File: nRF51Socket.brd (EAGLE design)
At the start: 46 x 41 mm, 11 parts, among them U1 QFN-48(52)BT-0.4-01-00, X1 16MHz

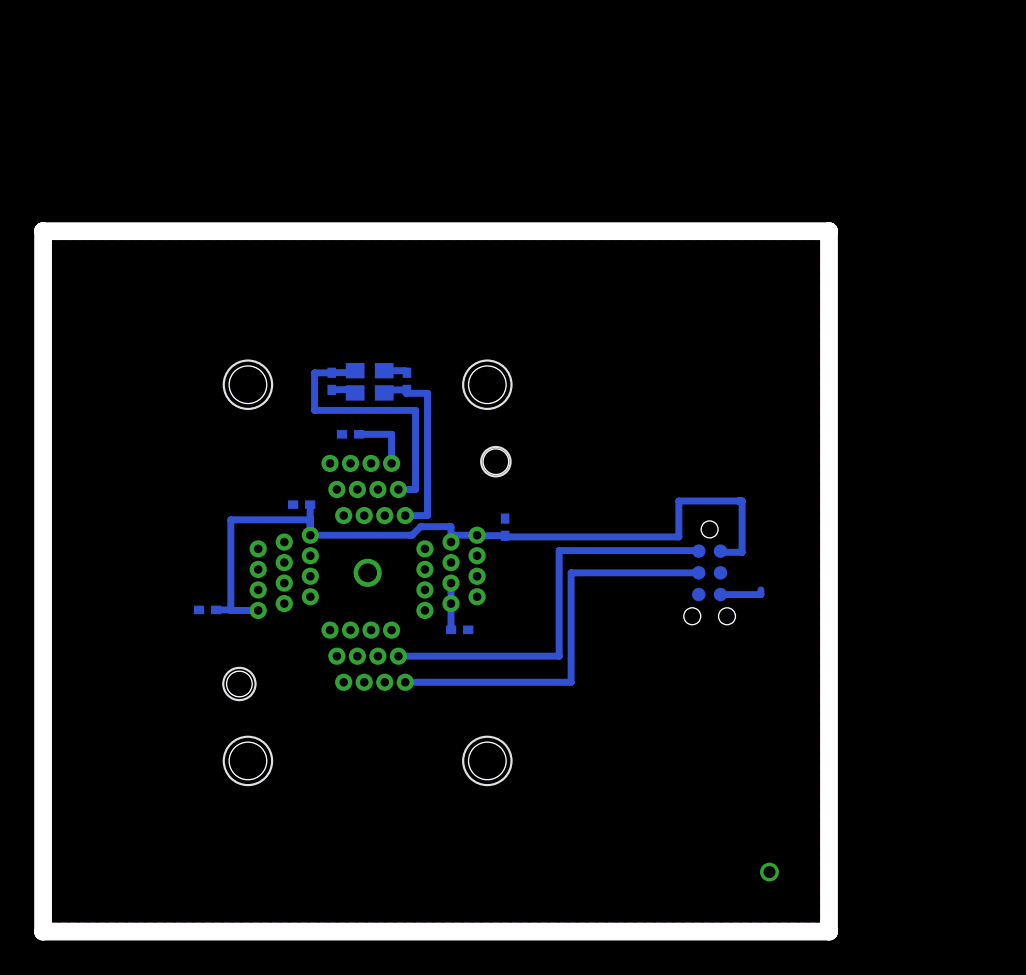
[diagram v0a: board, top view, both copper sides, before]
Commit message: Changed to 20pin jtag socket.
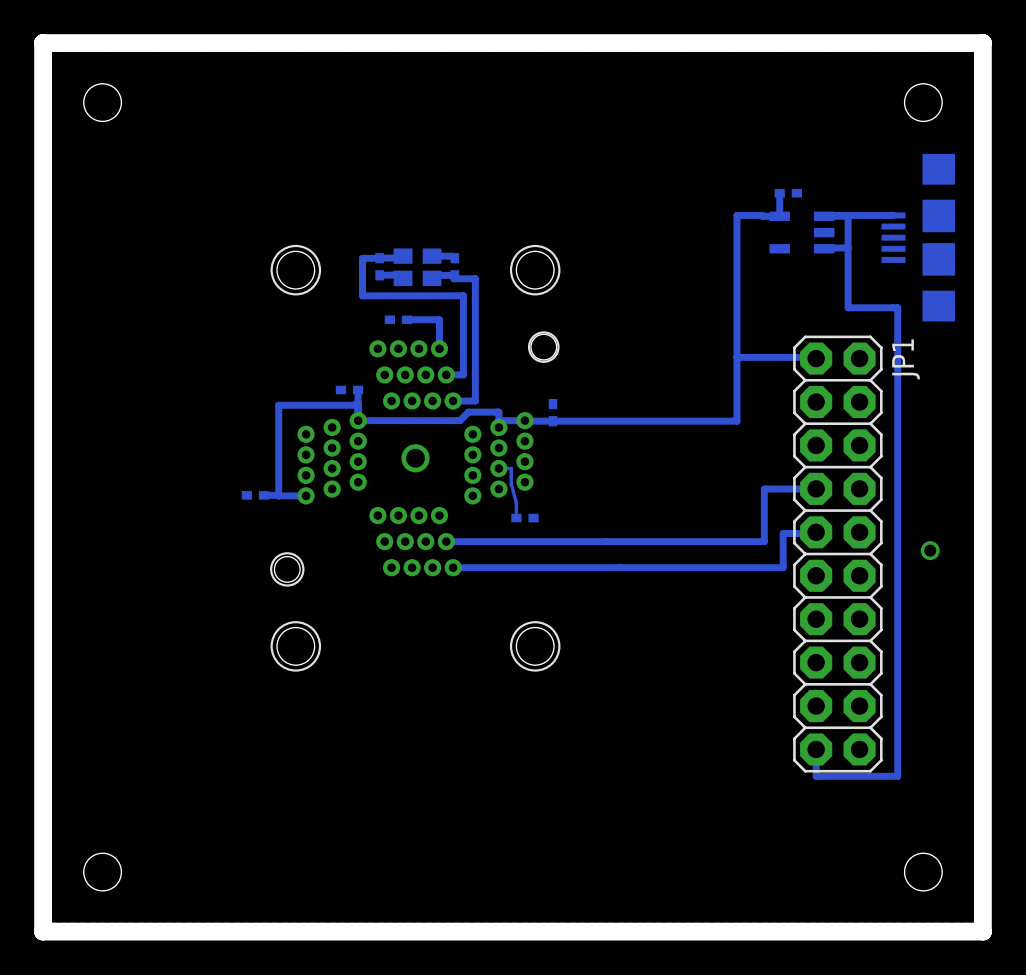
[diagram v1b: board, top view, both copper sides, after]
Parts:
- removed TC1: TC2030-IDC-NL, TagConnect:TC2030-IDC-NL
- added C18: 1uF, Nordic:CAP-403
- added FRAME2: FRAME-LETTERNO_PACKAGE, SparkFun-Aesthetics:DUMMY
- added JP1: (no value), SparkFun-Connectors:2X10
- added JP2: USB-MICROB, SparkFun-Connectors:USB-MICROB
- added U5: V_REG_LDOSMD, SparkFun-PowerIC:SOT23-5
- moved C2 7.57 mm to (27.7, 23.7)
- moved C4 7.26 mm to (11.9, 25.0)
- moved C5 7.26 mm to (17.4, 31.2)
- moved C3 7.26 mm to (29.3, 29.9)
- moved C7 7.26 mm to (19.2, 38.4)
- moved C8 7.26 mm to (23.6, 38.4)
- moved U1 7.26 mm to (21.3, 27.2)
- moved C6 7.26 mm to (20.3, 35.3)
- moved X1 7.26 mm to (21.4, 38.4)
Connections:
- removed net N$2: TC1.3
- new net VBUS: JP1.19, JP2.VBUS, U5.1, U5.3
- net 3.3V: now also C18.2, JP1.1, U5.5; no longer TC1.1
- net GND: now also C18.1, JP1.10, JP1.12, JP1.14, JP1.16, JP1.18, JP1.20, JP1.4, JP1.6, JP1.8, JP2.GND, JP2.MT1, JP2.MT2, U5.2; no longer TC1.5
- net SWDCLK: now also JP1.9; no longer TC1.4
- net SWDIO/!RESET: now also JP1.7; no longer TC1.2
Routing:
- net VBUS: track 0.00 -> 48.9 mm
- net 3.3V: track 49.0 -> 59.6 mm
- net GND: track 5.28 -> 2.65 mm
- net SWDIO/!RESET: track 23.8 -> 24.7 mm
- net N$1: track 2.73 -> 3.67 mm
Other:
- board size 46 x 41 mm -> 55 x 52 mm

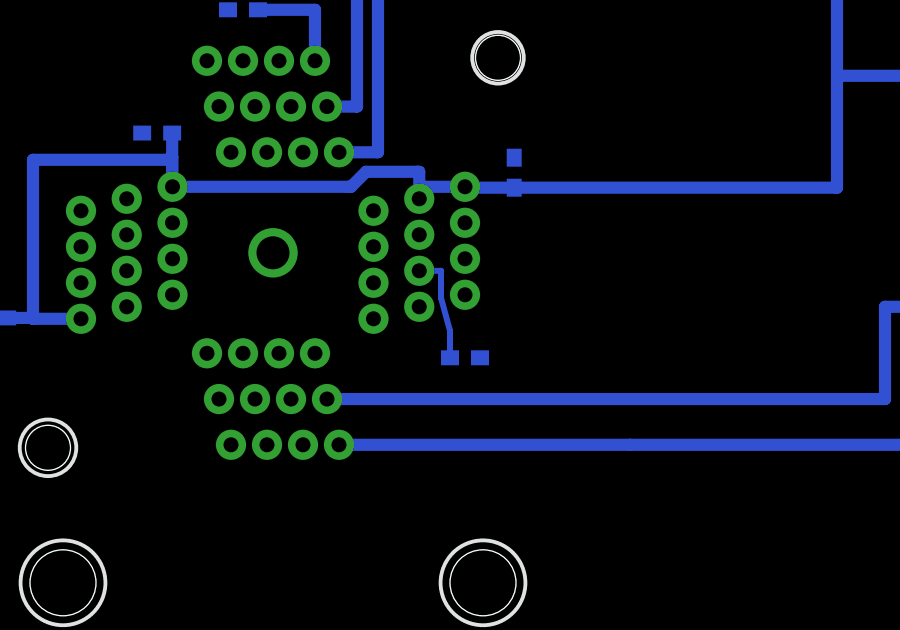
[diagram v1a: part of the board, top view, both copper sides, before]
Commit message: More routable trace location.
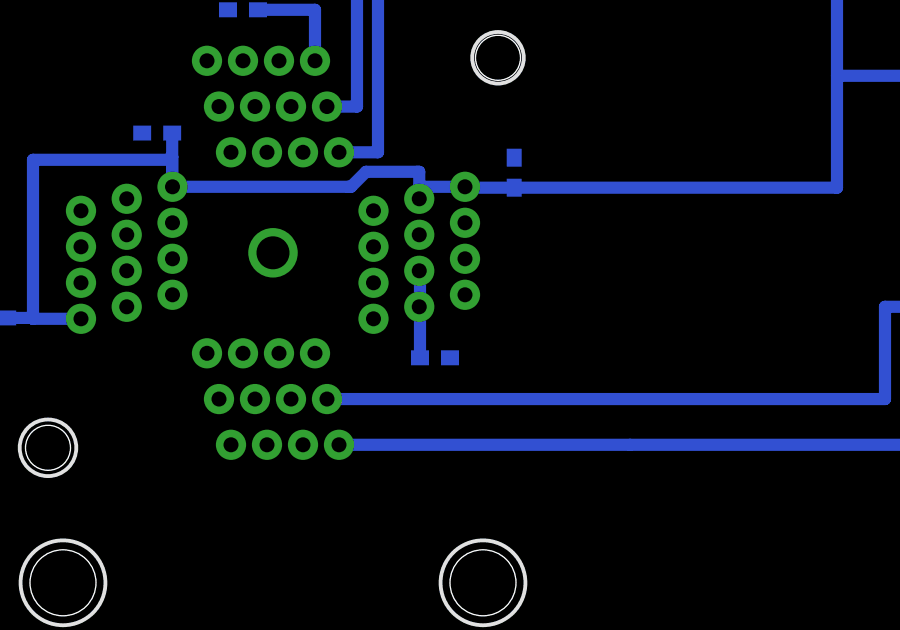
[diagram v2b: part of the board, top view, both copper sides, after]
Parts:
- moved C2 1.00 mm to (26.7, 23.7)
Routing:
- net N$1: track 3.67 -> 2.93 mm
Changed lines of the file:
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@@
 <?xml version="1.0" encoding="utf-8"?>
 <!DOCTYPE eagle SYSTEM "eagle.dtd">
-<eagle version="7.2.0">
+<eagle version="7.4.0">
 <drawing>
 <settings>
@@
 <setting verticaltext="up"/>
 </settings>
-<grid distance="1" unitdist="mm" unit="mm" style="lines" multiple="1" display="yes" altdistance="0.05" altunitdist="inch" altunit="inch"/>
+<grid distance="0.1" unitdist="mm" unit="mm" style="lines" multiple="1" display="yes" altdistance="0.05" altunitdist="inch" altunit="inch"/>
 <layers>
 <layer number="1" name="Top" color="4" fill="1" visible="yes" active="yes"/>
@@
 </autorouter>
 <elements>
-<element name="C2" library="Nordic" package="CAP-403" value="47nF" x="27.7" y="23.7" rot="MR0"/>
+<element name="C2" library="Nordic" package="CAP-403" value="47nF" x="26.7" y="23.7" rot="MR0"/>
 <element name="C3" library="Nordic" package="CAP-403" value="1nF" x="29.34" y="29.87" rot="MR270"/>
 <element name="C6" library="Nordic" package="CAP-403" value="100nF" x="20.3" y="35.3" rot="MR180"/>
@@
 <contactref element="C2" pad="2"/>
 <contactref element="U1" pad="DEC2"/>
-<wire x1="26.175" y1="26.6" x2="26.9" y2="26.6" width="0.2" layer="16"/>
-<wire x1="26.9" y1="26.6" x2="26.9" y2="25.7" width="0.2" layer="16"/>
-<wire x1="26.9" y1="25.7" x2="27.2" y2="24.6" width="0.2" layer="16"/>
-<wire x1="27.2" y1="24.6" x2="27.2" y2="24.5" width="0.2" layer="16"/>
-<wire x1="27.2" y1="24.5" x2="27.2" y2="23.7" width="0.2" layer="16"/>
+<wire x1="26.175" y1="26.6" x2="26.2" y2="26.6" width="0.4064" layer="16"/>
+<wire x1="26.2" y1="26.6" x2="26.2" y2="23.7" width="0.4064" layer="16"/>
 </signal>
 <signal name="SWDIO/!RESET">
